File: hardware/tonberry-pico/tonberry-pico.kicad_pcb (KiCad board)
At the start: 2 copper layers, 100 x 102 mm, 33 parts, among them J1 MicroSD_Breakout, J2 SparkFun I2S Audio Breakout M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, J3 RC522_Breakout, J4 Adafruit_bq25185_5V, J5 UART, J6 WS2812, J7 Buttons, Q1 2N7000, Q2 2N7000, SW1 SW_Push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

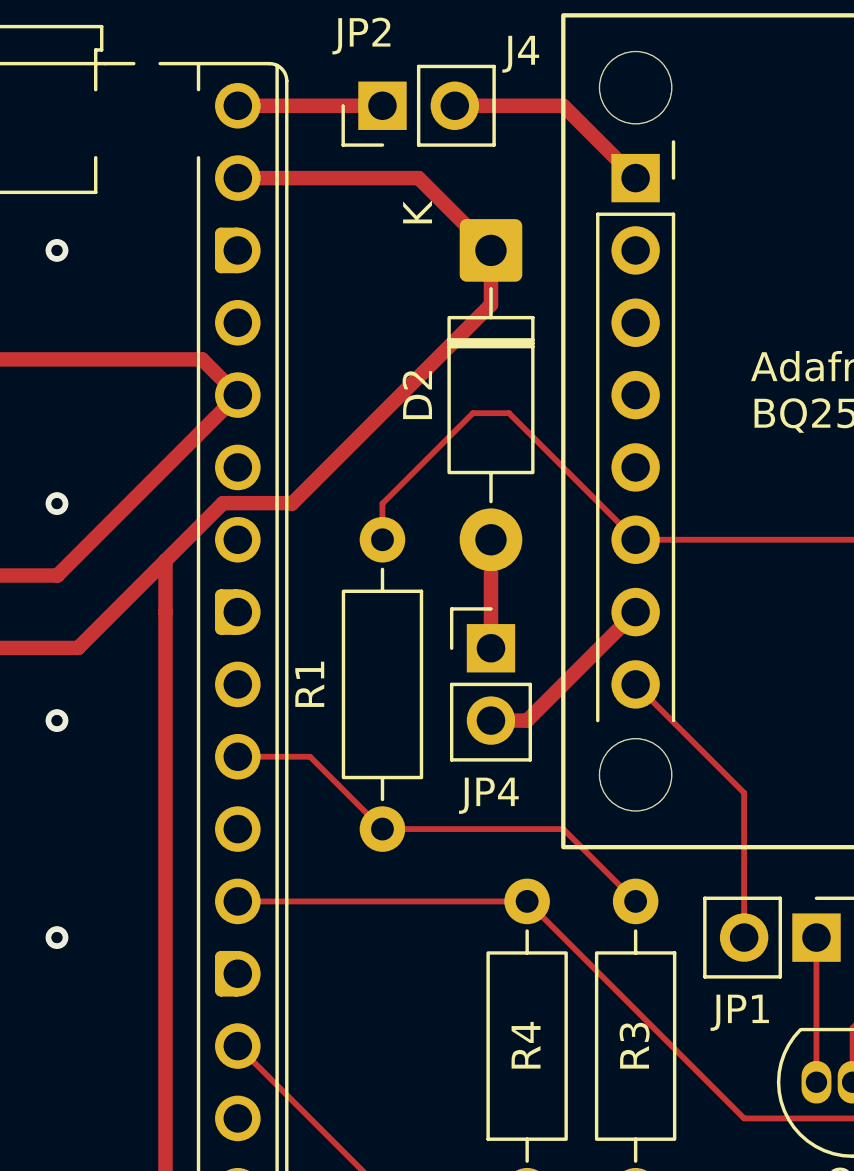
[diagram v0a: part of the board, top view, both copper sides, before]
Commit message: hw: Clean up schematic, add RUN reset
Clean up schematic and put battery power, buttons and run/reset in
subblocks.

Add missing switch on RUN to reset the RP2040. In the PCB this is
actually a jumper instead of a switch right now, so it fits in the
existing layout.

Signed-off-by: Matthias Blankertz <matthias@blankertz.org>
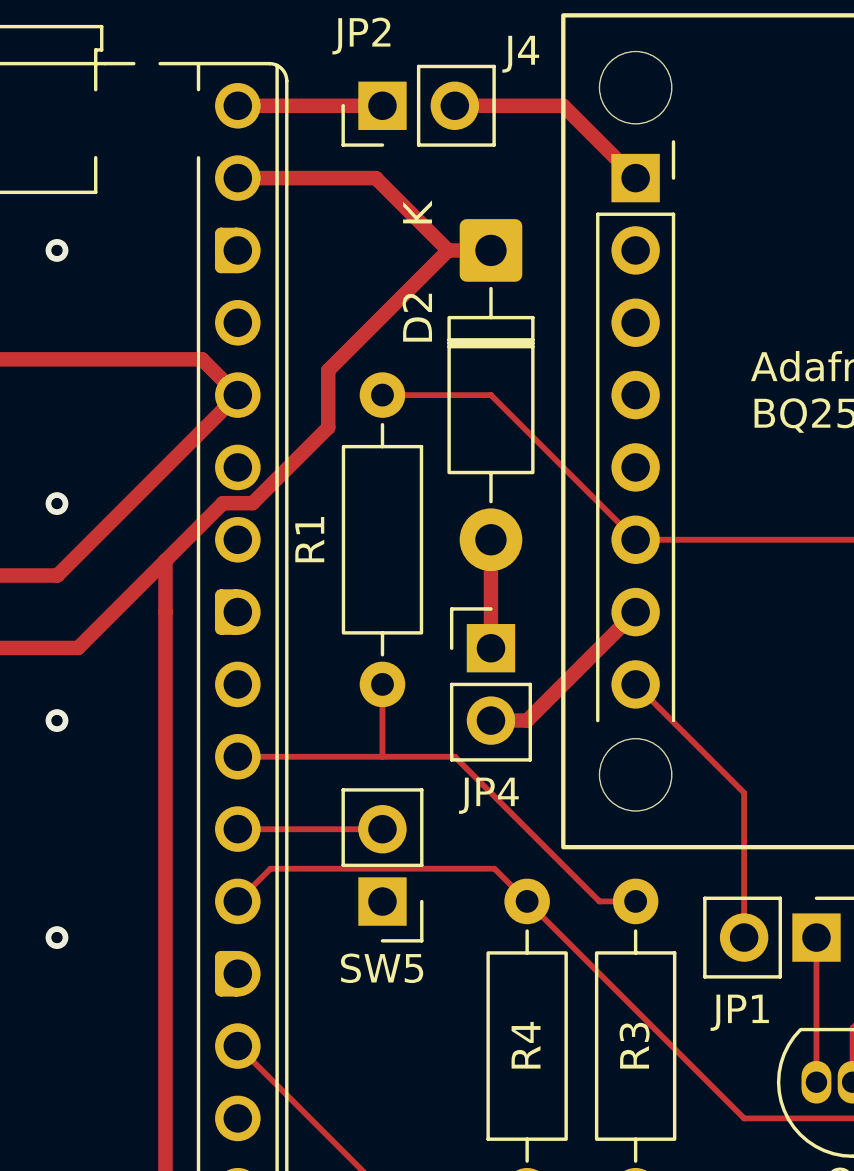
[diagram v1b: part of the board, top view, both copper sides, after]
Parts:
- added SW5: SW_Push, Connector_PinHeader_2.54mm:PinHeader_1x02_P2.54mm_Vertical, F.Cu at (181.6, 69.9)
- D1, D3: value D -> 1N4448
- D2: value D_Schottky -> 1N5817
- moved R1 5.08 mm to (181.6, 52.1)
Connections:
- net /+5V_BAT renamed /BQ_+5V
- net /D+ renamed /BQ_D+
- net /D- renamed /BQ_D-
- net /EN renamed /BQ_EN
- net /POWER_EN renamed /POWER_EN_RP
- net /VBAT renamed /BQ_VBAT
- net /VBUS renamed /BQ_VBUS
- net /VIN renamed /BQ_VIN
- net Net-(J7-Pin_3) renamed /BUTTON1
- net Net-(J7-Pin_4) renamed /BUTTON2
- net Net-(J7-Pin_5) renamed /BUTTON3
- net Net-(JP2-A) renamed VBUS
- D1 pad 1: Net-(D1-K) -> /POWER_BUTTON
- D1 pad 2: /POWER_BUTTON -> Net-(D1-A)
- D3 pad 1: Net-(D1-K) -> /POWER_BUTTON
- J7 pad 2: Net-(D1-K) -> /POWER_BUTTON
- SW4 pad 1: Net-(D1-K) -> /POWER_BUTTON
- U1 pad 27: /POWER_BUTTON -> Net-(D1-A)
- U1 pad 30: unconnected-(U1-RUN-Pad30) -> /RP_RUN
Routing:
- net Net-(D1-K): track 22.2 -> 0.00 mm
- net /POWER_BUTTON: track 10.3 -> 22.2 mm
- net Net-(D1-A): track 0.00 -> 10.3 mm
- net /RP_RUN: track 0.00 -> 5.08 mm
- net /VBAT_DIV_2: track 16.1 -> 18.6 mm
- net /BQ_VBAT: track 32.4 -> 30.0 mm
- net +5V: track 102.6 -> 101.1 mm
- net /POWER_EN_RP: track 33.0 -> 34.0 mm

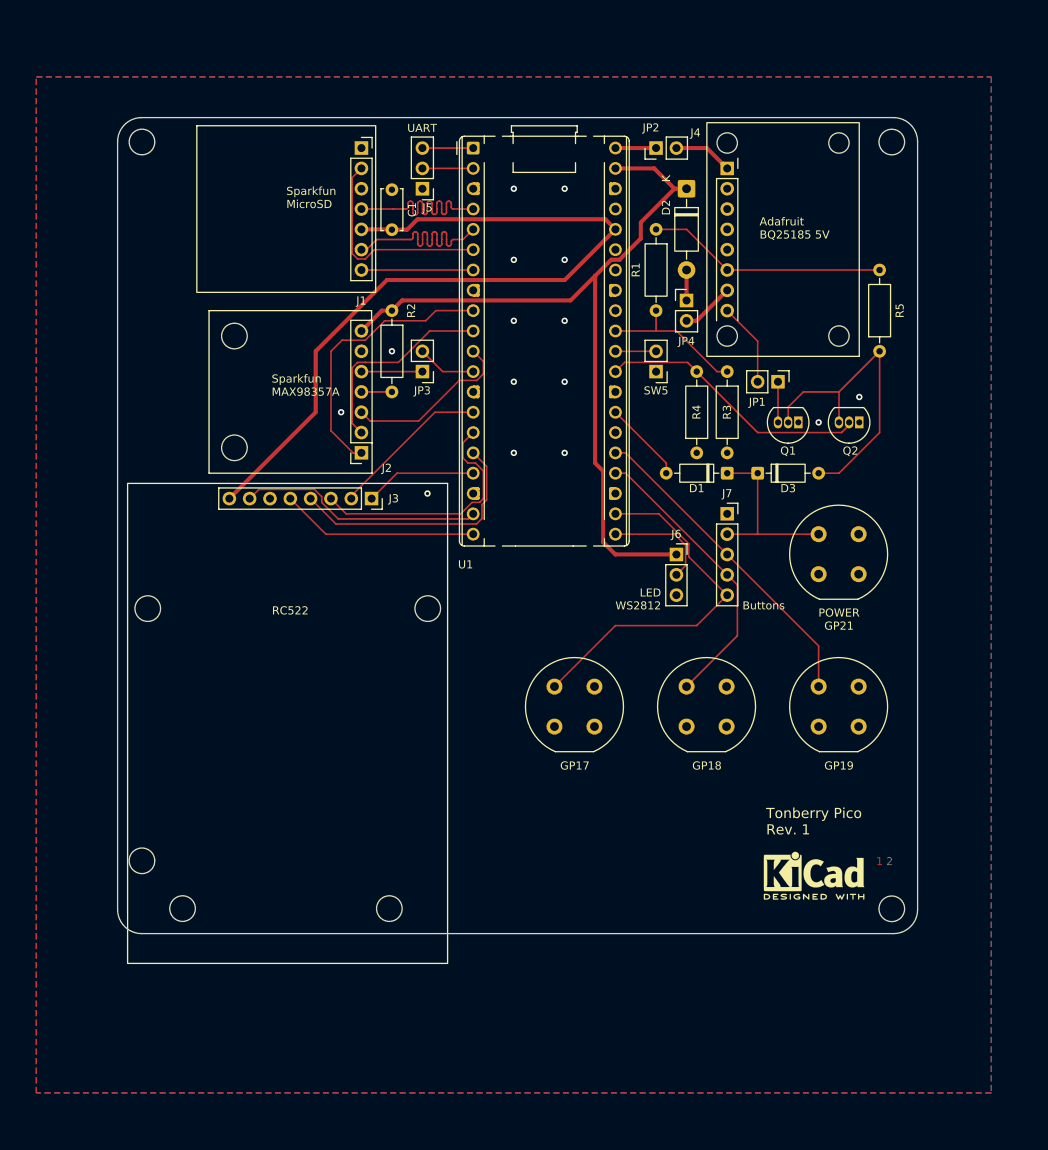
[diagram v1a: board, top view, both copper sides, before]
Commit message: hw: Use new and improved RPi Pico symbol in schematic
Signed-off-by: Matthias Blankertz <matthias@blankertz.org>
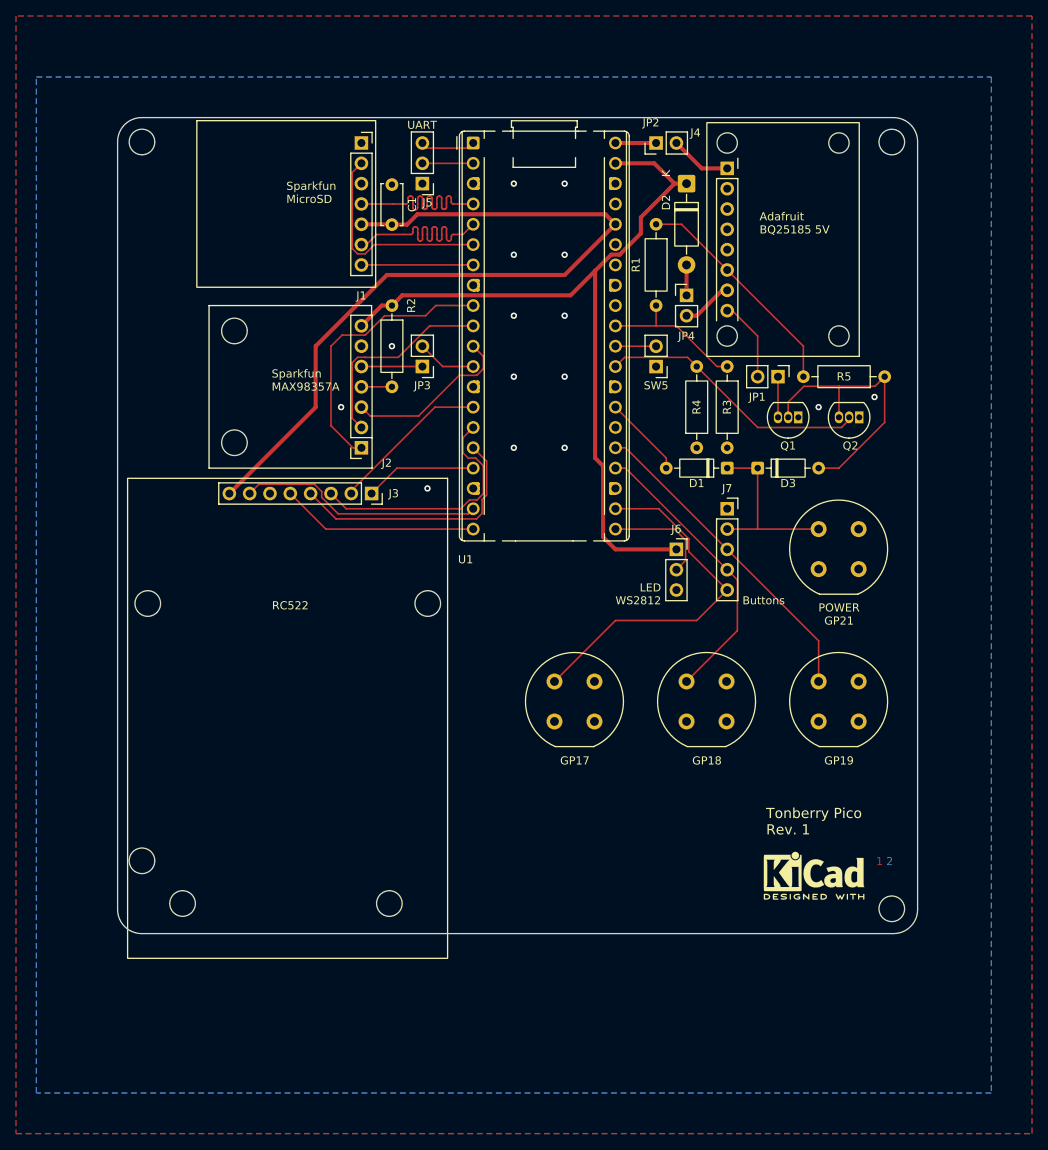
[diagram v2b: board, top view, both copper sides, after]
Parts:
- U1: value Pico -> RaspberryPi_Pico_W
- moved R5 3.24 mm to (210.2, 70.5), turned to 180 degrees
- moved D2 0.64 mm to (185.4, 46.4)
- moved J2 0.64 mm to (144.8, 79.4)
- moved J5 0.64 mm to (152.4, 46.4)
- moved JP1 0.64 mm to (196.8, 70.5)
- moved Q1 0.64 mm to (199.4, 75.6)
- moved Q2 0.64 mm to (207.0, 75.6)
- moved R4 0.64 mm to (186.7, 79.4)
- moved SW1 0.64 mm to (201.9, 108.6)
- moved SW2 0.64 mm to (185.4, 108.6)
- moved SW3 0.64 mm to (168.9, 108.6)
- moved SW4 0.64 mm to (201.9, 89.5)
- moved SW5 0.64 mm to (181.6, 69.2)
- moved C1 0.63 mm to (148.6, 51.5)
- moved J1 0.63 mm to (144.8, 41.3)
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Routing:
- net Net-(D3-A): track 39.9 -> 35.5 mm
- net /BQ_VBAT: track 30.0 -> 28.5 mm

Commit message: hw: Cleanup schematic style, fix ERC violations
No netlist changes.

Signed-off-by: Matthias Blankertz <matthias@blankertz.org>
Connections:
- net /BUTTON1 renamed BUTTON1
- net /BUTTON2 renamed BUTTON2
- net /BUTTON3 renamed BUTTON3
- net /POWER_BUTTON renamed POWER_BUTTON
- net /POWER_EN_RP renamed POWER_EN_RP
- net /RP_RUN renamed RP_RUN
- net /VBAT_DIV_2 renamed VBAT_DIV_2

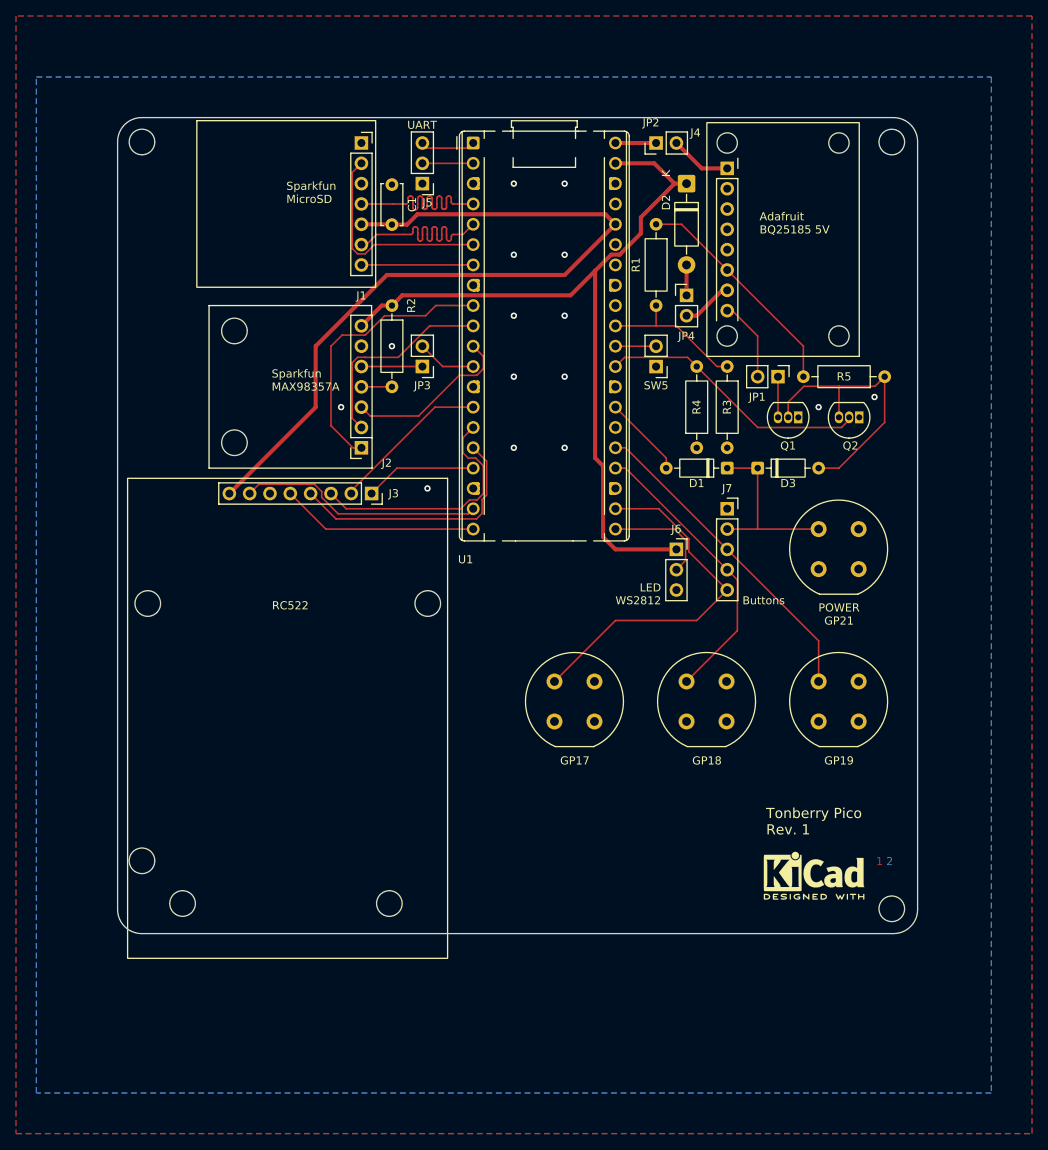
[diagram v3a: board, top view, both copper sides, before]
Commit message: hw: Add fifth button, make traces wider
Signed-off-by: Matthias Blankertz <matthias@blankertz.org>
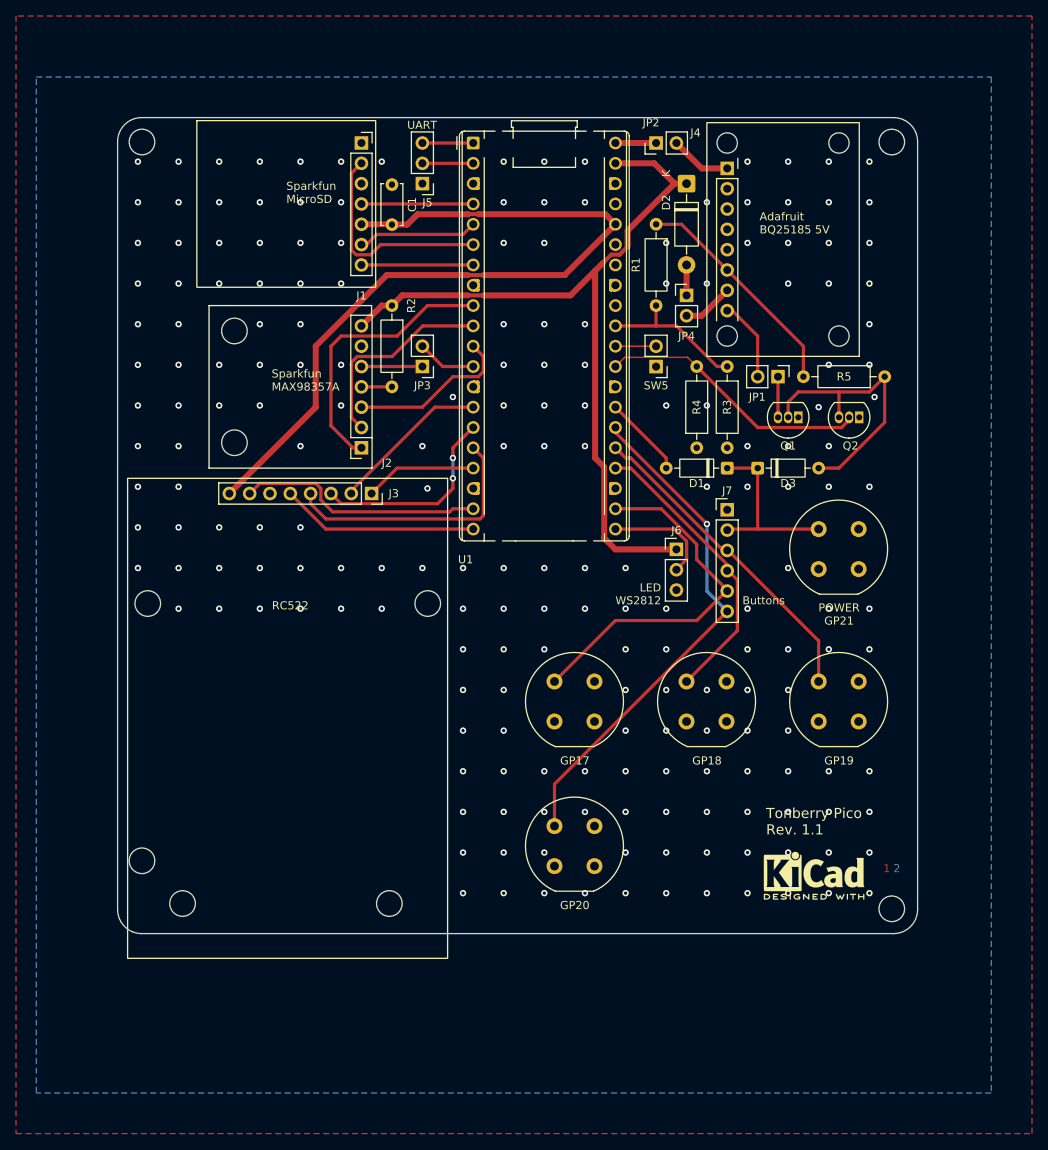
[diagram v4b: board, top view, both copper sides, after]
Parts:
- added SW6: SW_Push, Button_Switch_THT:Push_E-Switch_KS01Q01, F.Cu at (168.9, 126.7)
- J6: footprint Connector_PinSocket_2.54mm:PinSocket_1x03_P2.54mm_Vertical -> Connector_PinHeader_2.54mm:PinHeader_1x03_P2.54mm_Vertical
- J7: footprint Connector_PinSocket_2.54mm:PinSocket_1x05_P2.54mm_Vertical -> Connector_PinHeader_2.54mm:PinHeader_1x06_P2.54mm_Vertical
- moved REF** 1.26 mm to (210.4, 133.2)
- moved J7 0.13 mm to (190.5, 87.1)
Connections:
- U1 pad 26: unconnected-(U1-GPIO20-Pad26) -> BUTTON4
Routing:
- net BUTTON4: track 0.00 -> 64.6 mm, vias 0 -> 1
- net /SD_SCK: track 26.8 -> 14.0 mm
- net /SD_DI: track 26.9 -> 15.0 mm
- net /RC522_MOSI: track 31.0 -> 25.2 mm, vias 0 -> 2
- net /I2S_DIN: track 21.5 -> 20.8 mm
- net Net-(D3-A): track 35.5 -> 34.8 mm
- net /RC522_MISO: track 32.2 -> 32.8 mm
- net GND: vias 15 -> 202
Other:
- board text added: "GP20"
- board text added: "Tonberry Pico Rev. 1.1"
- board text removed: "Tonberry Pico Rev. 1"

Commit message: hw: Smaller 'production' version of board w/o keys and direct RC522 mount
Signed-off-by: Matthias Blankertz <matthias@blankertz.org>
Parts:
- removed the REF** at (211.1, 137.0)
- removed the REF** at (117.3, 131.0)
- removed SW1, SW2, SW3, SW4, SW6: SW_Push, Button_Switch_THT:Push_E-Switch_KS01Q01
- added REF**: MountingHole_3.2mm_M3_DIN965, MountingHole:MountingHole_3.2mm_M3_DIN965, F.Cu at (212.7, 88.3)
- added REF**: MountingHole_3.2mm_M3_DIN965, MountingHole:MountingHole_3.2mm_M3_DIN965, F.Cu at (121.3, 88.1)
- J3: footprint Modules:AZ_Delivery_RC522 -> Connector_PinSocket_2.54mm:PinSocket_1x08_P2.54mm_Vertical
- J6: footprint Connector_PinHeader_2.54mm:PinHeader_1x03_P2.54mm_Vertical -> Connector_JST:JST_XH_B3B-XH-A_1x03_P2.50mm_Vertical
- J7: footprint Connector_PinHeader_2.54mm:PinHeader_1x06_P2.54mm_Vertical -> Connector_JST:JST_XH_B6B-XH-A_1x06_P2.50mm_Vertical
- Q1, Q2: footprint Package_TO_SOT_THT:TO-92_Inline -> Package_TO_SOT_THT:TO-92_Inline_Wide
- SW5: footprint Connector_PinHeader_2.54mm:PinHeader_1x02_P2.54mm_Vertical -> PCM_JLCPCB:SW_TS-1088-AR02016
- moved REF** 103.1 mm to (121.9, 67.2), turned to 90 degrees
- moved REF** 50.2 mm to (212.0, 83.1)
- moved J6 5.06 mm to (182.3, 87.4)
- moved REF** 3.95 mm to (121.3, 41.1)
- moved J7 3.16 mm to (193.6, 87.4)
- moved REF** 1.66 mm to (212.7, 41.3)
- moved SW5 1.28 mm to (181.5, 67.9), turned to 90 degrees
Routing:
- net BUTTON4: track 64.6 -> 35.2 mm, vias 1 -> 0
- net BUTTON1: track 40.5 -> 26.2 mm
- net POWER_BUTTON: track 22.2 -> 9.66 mm
- net BUTTON3: track 45.6 -> 34.4 mm
- net BUTTON2: track 36.7 -> 31.6 mm
- net +5V: track 101.1 -> 96.6 mm
- net Net-(J6-Pin_2): track 13.6 -> 10.4 mm
- net Net-(JP1-A): track 5.08 -> 6.13 mm
- net RP_RUN: track 5.08 -> 5.93 mm
- net Net-(D3-A): track 34.8 -> 35.5 mm
- net GND: vias 202 -> 104
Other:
- board size 100 x 102 mm -> 98 x 53.5 mm
- board text added: "RESET"
- board text added: "Tonberry Pico Rev. 1.2"
- board text removed: "GP17"
- board text removed: "GP18"
- board text removed: "GP19"
- board text removed: "GP20"
- board text removed: "POWER GP21"
- board text removed: "Tonberry Pico Rev. 1.1"
